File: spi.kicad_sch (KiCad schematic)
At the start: 23 parts, among them CN5 THERMO1, CN6 THERMO2, IC2 MAX31855K, IC3 MAX31855K, IC4 MCP2515-xSO, IC5 TCAN332DR, J3 CAN_TERM, J4 6_PIN_MOL_MICROFIT, T6 TEST_CAN, Y1 8MHz

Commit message: All review changes complete, except update CAN connector
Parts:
- removed CAN1, CAN2: Conn_01x03, Library:CONN_SD-43650-001_03_MOL, symbol Connector_Generic:Conn_01x03
- added CAN3, CAN4: Conn_01x03, Library:CONN_SD-43650-001_03_MOL, symbol Connector_Generic:Conn_01x03
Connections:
- net CANH: now also CAN3.2 (Pin_2), CAN4.2 (Pin_2)
- net CANL: now also CAN3.1 (Pin_1), CAN4.1 (Pin_1)
- net GND: now also CAN3.3 (Pin_3), CAN4.3 (Pin_3)
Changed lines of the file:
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@@
 	)
 	(junction
-		(at 266.7 118.11)
+		(at 72.39 101.6)
 		(diameter 0)
 		(color 0 0 0 0)
 	)
 	(junction
-		(at 72.39 101.6)
+		(at 86.36 184.15)
 		(diameter 0)
 		(color 0 0 0 0)
 	)
 	(junction
-		(at 86.36 184.15)
+		(at 266.7 118.11)
 		(diameter 0)
 		(color 0 0 0 0)
@@
 	(wire
 		(pts
-			(xy 270.51 123.19) (xy 270.51 142.24)
-		)
-		(stroke
-			(width 0)
-			(type default)
-		)
-	)
-	(wire
-		(pts
 			(xy 207.01 55.88) (xy 203.2 55.88)
 		)
@@
 	(wire
 		(pts
+			(xy 270.51 123.19) (xy 270.51 142.24)
+		)
+		(stroke
+			(width 0)
+			(type default)
+		)
+	)
+	(wire
+		(pts
 			(xy 63.5 104.14) (xy 63.5 109.22)
 		)
@@
 	(symbol
 		(lib_id "Connector_Generic:Conn_01x03")
-		(at 279.4 139.7 0)
+		(at 279.4 120.65 0)
 		(unit 1)
 		(exclude_from_sim no)
@@
 		(dnp no)
 		(fields_autoplaced yes)
-		(property "Reference" "CAN2"
-			(at 281.94 138.4299 0)
+		(property "Reference" "CAN3"
+			(at 281.94 119.3799 0)
 			(effects
 				(font
@@
 		)
 		(property "Value" "Conn_01x03"
-			(at 281.94 140.9699 0)
+			(at 281.94 121.9199 0)
 			(effects
 				(font
@@
 		)
 		(property "Footprint" "Library:CONN_SD-43650-001_03_MOL"
-			(at 279.4 139.7 0)
+			(at 279.4 120.65 0)
 			(effects
 				(font
@@
 		)
 		(property "Datasheet" "~"
-			(at 279.4 139.7 0)
+			(at 279.4 120.65 0)
 			(effects
 				(font
@@
 		)
 		(property "Description" "Generic connector, single row, 01x03, script generated (kicad-library-utils/schlib/autogen/connector/)"
-			(at 279.4 139.7 0)
+			(at 279.4 120.65 0)
 			(effects
 				(font
@@
 			(project "telemetry-pcb"
 				(path "/871fe08d-2afd-493a-a8ef-c8aa2cbbb7b9/00000000-0000-0000-0000-00006195e29d"
-					(reference "CAN2")
+					(reference "CAN3")
 					(unit 1)
 				)
@@
 	(symbol
 		(lib_id "Connector_Generic:Conn_01x03")
-		(at 279.4 120.65 0)
+		(at 279.4 139.7 0)
 		(unit 1)
 		(exclude_from_sim no)
@@
 		(dnp no)
 		(fields_autoplaced yes)
-		(property "Reference" "CAN1"
-			(at 281.94 119.3799 0)
+		(property "Reference" "CAN4"
+			(at 281.94 138.4299 0)
 			(effects
 				(font
@@
 		)
 		(property "Value" "Conn_01x03"
-			(at 281.94 121.9199 0)
+			(at 281.94 140.9699 0)
 			(effects
 				(font
@@
 		)
 		(property "Footprint" "Library:CONN_SD-43650-001_03_MOL"
-			(at 279.4 120.65 0)
+			(at 279.4 139.7 0)
 			(effects
 				(font
@@
 		)
 		(property "Datasheet" "~"
-			(at 279.4 120.65 0)
+			(at 279.4 139.7 0)
 			(effects
 				(font
@@
 		)
 		(property "Description" "Generic connector, single row, 01x03, script generated (kicad-library-utils/schlib/autogen/connector/)"
-			(at 279.4 120.65 0)
+			(at 279.4 139.7 0)
 			(effects
 				(font
@@
 		)
 		(instances
-			(project ""
+			(project "telemetry-pcb"
 				(path "/871fe08d-2afd-493a-a8ef-c8aa2cbbb7b9/00000000-0000-0000-0000-00006195e29d"
-					(reference "CAN1")
+					(reference "CAN4")
 					(unit 1)
 				)

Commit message: Backup
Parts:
- added CAN1, Can2: 39301040, CONN_5569-04A_MOL, symbol 2025-11-01_18-29-52:39301040
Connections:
- net CANH: now also CAN1.2, Can2.2; no longer CAN3.2 (Pin_2), CAN4.2 (Pin_2)
- net CANL: now also CAN1.1, Can2.1; no longer CAN3.1 (Pin_1), CAN4.1 (Pin_1)
- net GND: now also CAN1.3, CAN1.4, Can2.3, Can2.4; no longer CAN3.3 (Pin_3), CAN4.3 (Pin_3)
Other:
- moved on the sheet: CAN3, CAN4
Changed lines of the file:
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@@
 	)
 	(junction
+		(at 270.51 144.78)
+		(diameter 0)
+		(color 0 0 0 0)
+	)
+	(junction
 		(at 227.33 118.11)
 		(diameter 0)
@@
 		(color 0 0 0 0)
 	)
+	(junction
+		(at 270.51 125.73)
+		(diameter 0)
+		(color 0 0 0 0)
+	)
 	(no_connect
 		(at 130.81 176.53)
@@
 	(wire
 		(pts
+			(xy 270.51 144.78) (xy 274.32 144.78)
+		)
+		(stroke
+			(width 0)
+			(type default)
+		)
+	)
+	(wire
+		(pts
 			(xy 243.84 118.11) (xy 266.7 118.11)
 		)
@@
 	(wire
 		(pts
+			(xy 270.51 125.73) (xy 270.51 142.24)
+		)
+		(stroke
+			(width 0)
+			(type default)
+		)
+	)
+	(wire
+		(pts
 			(xy 66.04 151.13) (xy 66.04 156.21)
 		)
@@
 	(wire
 		(pts
+			(xy 270.51 144.78) (xy 270.51 153.67)
+		)
+		(stroke
+			(width 0)
+			(type default)
+		)
+	)
+	(wire
+		(pts
 			(xy 127 99.06) (xy 127 48.26)
 		)
@@
 	(wire
 		(pts
-			(xy 270.51 123.19) (xy 270.51 142.24)
+			(xy 270.51 123.19) (xy 270.51 125.73)
 		)
 		(stroke
@@
 	(wire
 		(pts
-			(xy 270.51 142.24) (xy 270.51 153.67)
+			(xy 270.51 142.24) (xy 270.51 144.78)
 		)
 		(stroke
@@
 	(wire
 		(pts
+			(xy 270.51 125.73) (xy 274.32 125.73)
+		)
+		(stroke
+			(width 0)
+			(type default)
+		)
+	)
+	(wire
+		(pts
 			(xy 227.33 133.35) (xy 227.33 132.08)
 		)
@@
 	)
 	(symbol
+		(lib_id "2025-11-01_18-29-52:39301040")
+		(at 287.02 147.32 0)
+		(unit 1)
+		(exclude_from_sim no)
+		(in_bom yes)
+		(on_board yes)
+		(dnp no)
+		(fields_autoplaced yes)
+		(property "Reference" "Can2"
+			(at 288.29 139.6999 0)
+			(effects
+				(font
+					(size 1.524 1.524)
+				)
+				(justify left)
+			)
+		)
+		(property "Value" "39301040"
+			(at 288.29 142.2399 0)
+			(effects
+				(font
+					(size 1.524 1.524)
+				)
+				(justify left)
+			)
+		)
+		(property "Footprint" "CONN_5569-04A_MOL"
+			(at 274.32 137.16 0)
+			(effects
+				(font
+					(size 1.27 1.27)
+					(italic yes)
+				)
+				(hide yes)
+			)
+		)
+		(property "Datasheet" "https://www.molex.com/en-us/products/part-detail-pdf/39301040?display=pdf"
+			(at 274.32 137.16 0)
+			(effects
+				(font
+					(size 1.27 1.27)
+					(italic yes)
+				)
+				(hide yes)
+			)
+		)
+		(property "Description" ""
+			(at 287.02 147.32 0)
+			(effects
+				(font
+					(size 1.27 1.27)
+				)
+				(hide yes)
+			)
+		)
+		(pin "2"
+		)
+		(pin "3"
+		)
+		(pin "1"
+		)
+		(pin "4"
+		)
+		(instances
+			(project "telemetry-pcb"
+				(path "/871fe08d-2afd-493a-a8ef-c8aa2cbbb7b9/00000000-0000-0000-0000-00006195e29d"
+					(reference "Can2")
+					(unit 1)
+				)
+			)
+		)
+	)
+	(symbol
 		(lib_id "telemetry_3.0_sch_library:6_PIN_MOL_MICROFIT")
 		(at 207.01 43.18 0)
@@
 	(symbol
 		(lib_id "Connector_Generic:Conn_01x03")
-		(at 279.4 120.65 0)
+		(at 283.21 88.9 0)
 		(unit 1)
 		(exclude_from_sim no)
@@
 		(fields_autoplaced yes)
 		(property "Reference" "CAN3"
-			(at 281.94 119.3799 0)
+			(at 285.75 87.6299 0)
 			(effects
 				(font
@@
 		)
 		(property "Value" "Conn_01x03"
-			(at 281.94 121.9199 0)
+			(at 285.75 90.1699 0)
 			(effects
 				(font
@@
 		)
 		(property "Footprint" "Library:CONN_SD-43650-001_03_MOL"
-			(at 279.4 120.65 0)
+			(at 283.21 88.9 0)
 			(effects
 				(font
@@
 		)
 		(property "Datasheet" "~"
-			(at 279.4 120.65 0)
+			(at 283.21 88.9 0)
 			(effects
 				(font
@@
 		)
 		(property "Description" "Generic connector, single row, 01x03, script generated (kicad-library-utils/schlib/autogen/connector/)"
-			(at 279.4 120.65 0)
+			(at 283.21 88.9 0)
 			(effects
 				(font
@@
 	(symbol
 		(lib_id "Connector_Generic:Conn_01x03")
-		(at 279.4 139.7 0)
+		(at 283.21 107.95 0)
 		(unit 1)
 		(exclude_from_sim no)
@@
 		(fields_autoplaced yes)
 		(property "Reference" "CAN4"
-			(at 281.94 138.4299 0)
+			(at 285.75 106.6799 0)
 			(effects
 				(font
@@
 		)
 		(property "Value" "Conn_01x03"
-			(at 281.94 140.9699 0)
+			(at 285.75 109.2199 0)
 			(effects
 				(font
@@
 		)
 		(property "Footprint" "Library:CONN_SD-43650-001_03_MOL"
-			(at 279.4 139.7 0)
+			(at 283.21 107.95 0)
 			(effects
 				(font
@@
 		)
 		(property "Datasheet" "~"
-			(at 279.4 139.7 0)
+			(at 283.21 107.95 0)
 			(effects
 				(font
@@
 		)
 		(property "Description" "Generic connector, single row, 01x03, script generated (kicad-library-utils/schlib/autogen/connector/)"
-			(at 279.4 139.7 0)
+			(at 283.21 107.95 0)
 			(effects
 				(font
@@
 					(unit 1)
 				)
+			)
+		)
+	)
+	(symbol
+		(lib_id "2025-11-01_18-29-52:39301040")
+		(at 287.02 128.27 0)
+		(unit 1)
+		(exclude_from_sim no)
+		(in_bom yes)
+		(on_board yes)
+		(dnp no)
+		(fields_autoplaced yes)
+		(property "Reference" "CAN1"
+			(at 288.29 120.6499 0)
+			(effects
+				(font
+					(size 1.524 1.524)
+				)
+				(justify left)
+			)
+		)
+		(property "Value" "39301040"
+			(at 288.29 123.1899 0)
+			(effects
+				(font
+					(size 1.524 1.524)
+				)
+				(justify left)
+			)
+		)
+		(property "Footprint" "CONN_5569-04A_MOL"
+			(at 274.32 118.11 0)
+			(effects
+				(font
+					(size 1.27 1.27)
+					(italic yes)
+				)
+				(hide yes)
+			)
+		)
+		(property "Datasheet" "https://www.molex.com/en-us/products/part-detail-pdf/39301040?display=pdf"
+			(at 274.32 118.11 0)
+			(effects
+				(font
+					(size 1.27 1.27)
+					(italic yes)
+				)
+				(hide yes)
+			)
+		)
+		(property "Description" ""
+			(at 287.02 128.27 0)
+			(effects
+				(font
+					(size 1.27 1.27)
+				)
+				(hide yes)
+			)
+		)
+		(pin "2"
+		)
+		(pin "3"
+		)
+		(pin "1"
+		)
+		(pin "4"
+		)
+		(instances
+			(project ""
+				(path "/871fe08d-2afd-493a-a8ef-c8aa2cbbb7b9/00000000-0000-0000-0000-00006195e29d"
+					(reference "CAN1")
+					(unit 1)
+				)

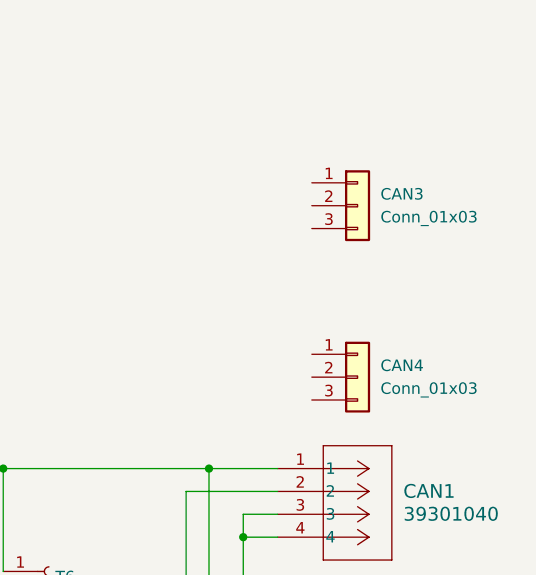
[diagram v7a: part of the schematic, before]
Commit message: connector changes
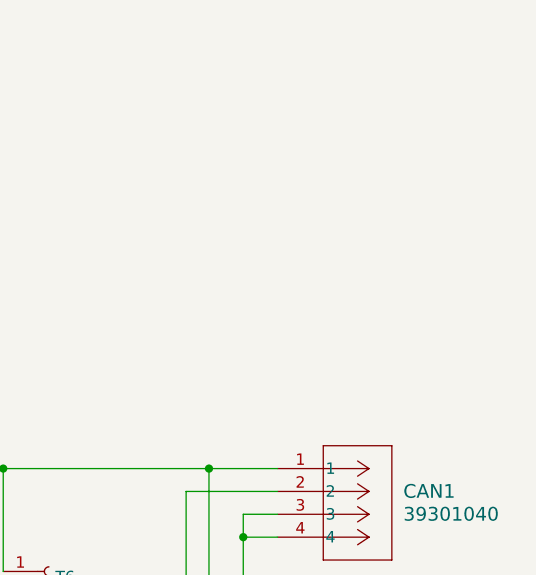
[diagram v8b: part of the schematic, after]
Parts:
- removed CAN3, CAN4: Conn_01x03, Library:CONN_SD-43650-001_03_MOL, symbol Connector_Generic:Conn_01x03
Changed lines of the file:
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@@
-	)
-	(symbol
-		(lib_id "Connector_Generic:Conn_01x03")
-		(at 283.21 88.9 0)
-		(unit 1)
-		(exclude_from_sim no)
-		(in_bom yes)
-		(on_board yes)
-		(dnp no)
-		(fields_autoplaced yes)
-		(property "Reference" "CAN3"
-			(at 285.75 87.6299 0)
-			(effects
-				(font
-					(size 1.27 1.27)
-				)
-				(justify left)
-			)
-		)
-		(property "Value" "Conn_01x03"
-			(at 285.75 90.1699 0)
-			(effects
-				(font
-					(size 1.27 1.27)
-				)
-				(justify left)
-			)
-		)
-		(property "Footprint" "Library:CONN_SD-43650-001_03_MOL"
-			(at 283.21 88.9 0)
-			(effects
-				(font
-					(size 1.27 1.27)
-				)
-				(hide yes)
-			)
-		)
-		(property "Datasheet" "~"
-			(at 283.21 88.9 0)
-			(effects
-				(font
-					(size 1.27 1.27)
-				)
-				(hide yes)
-			)
-		)
-		(property "Description" "Generic connector, single row, 01x03, script generated (kicad-library-utils/schlib/autogen/connector/)"
-			(at 283.21 88.9 0)
-			(effects
-				(font
-					(size 1.27 1.27)
-				)
-				(hide yes)
-			)
-		)
-		(pin "1"
-		)
-		(pin "3"
-		)
-		(pin "2"
-		)
-		(instances
-			(project "telemetry-pcb"
-				(path "/871fe08d-2afd-493a-a8ef-c8aa2cbbb7b9/00000000-0000-0000-0000-00006195e29d"
-					(reference "CAN3")
-					(unit 1)
-				)
-			)
-		)
-	)
-	(symbol
-		(lib_id "Connector_Generic:Conn_01x03")
-		(at 283.21 107.95 0)
-		(unit 1)
-		(exclude_from_sim no)
-		(in_bom yes)
-		(on_board yes)
-		(dnp no)
-		(fields_autoplaced yes)
-		(property "Reference" "CAN4"
-			(at 285.75 106.6799 0)
-			(effects
-				(font
-					(size 1.27 1.27)
-				)
-				(justify left)
-			)
-		)
-		(property "Value" "Conn_01x03"
-			(at 285.75 109.2199 0)
-			(effects
-				(font
-					(size 1.27 1.27)
-				)
-				(justify left)
-			)
-		)
-		(property "Footprint" "Library:CONN_SD-43650-001_03_MOL"
-			(at 283.21 107.95 0)
-			(effects
-				(font
-					(size 1.27 1.27)
-				)
-				(hide yes)
-			)
-		)
-		(property "Datasheet" "~"
-			(at 283.21 107.95 0)
-			(effects
-				(font
-					(size 1.27 1.27)
-				)
-				(hide yes)
-			)
-		)
-		(property "Description" "Generic connector, single row, 01x03, script generated (kicad-library-utils/schlib/autogen/connector/)"
-			(at 283.21 107.95 0)
-			(effects
-				(font
-					(size 1.27 1.27)
-				)
-				(hide yes)
-			)
-		)
-		(pin "1"
-		)
-		(pin "3"
-		)
-		(pin "2"
-		)
-		(instances
-			(project "telemetry-pcb"
-				(path "/871fe08d-2afd-493a-a8ef-c8aa2cbbb7b9/00000000-0000-0000-0000-00006195e29d"
-					(reference "CAN4")
-					(unit 1)
-				)
-			)
-		)
 	)
 	(symbol
